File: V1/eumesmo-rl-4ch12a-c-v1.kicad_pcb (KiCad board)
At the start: 2 copper layers, 68 x 67.8 mm, 29 parts, among them J1 250-202, J2 250-204, J3 DB142V-5.08-6P, J4 DB142V-5.08-6P, K1 Songle_SRD_1C, K2 Songle_SRD_1C, K3 Songle_SRD_1C, K4 Songle_SRD_1C

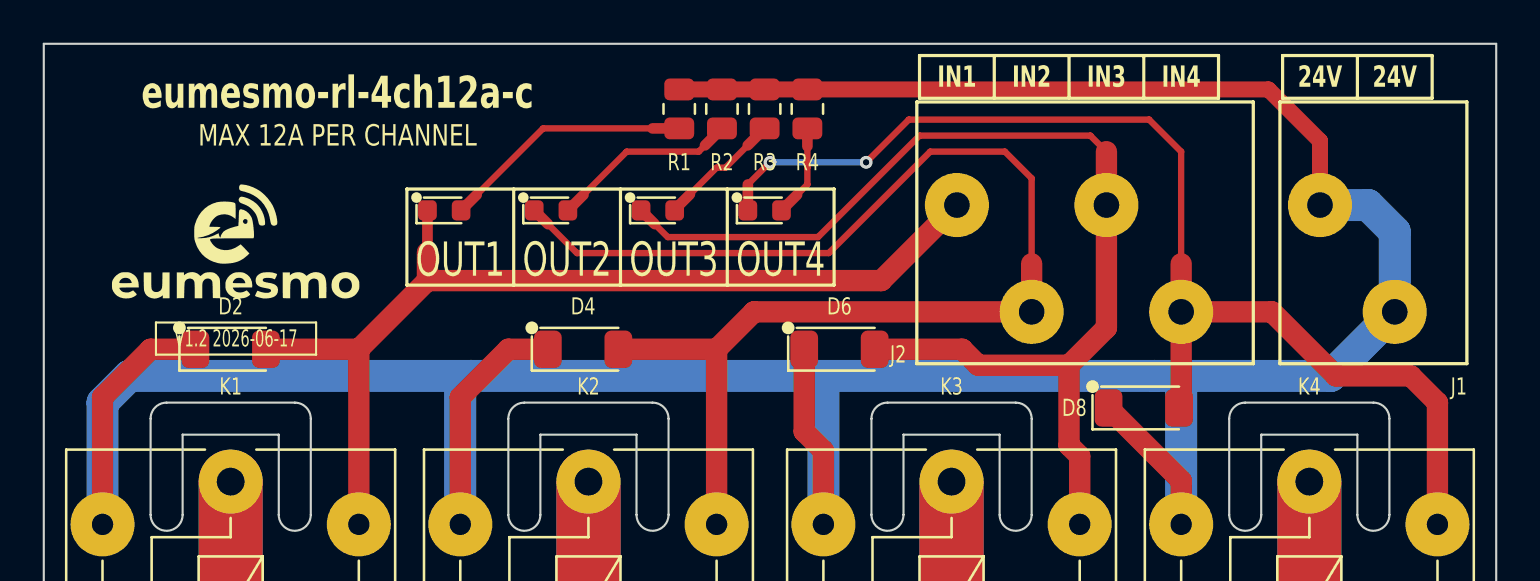
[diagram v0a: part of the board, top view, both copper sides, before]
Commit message: Repo renamed.
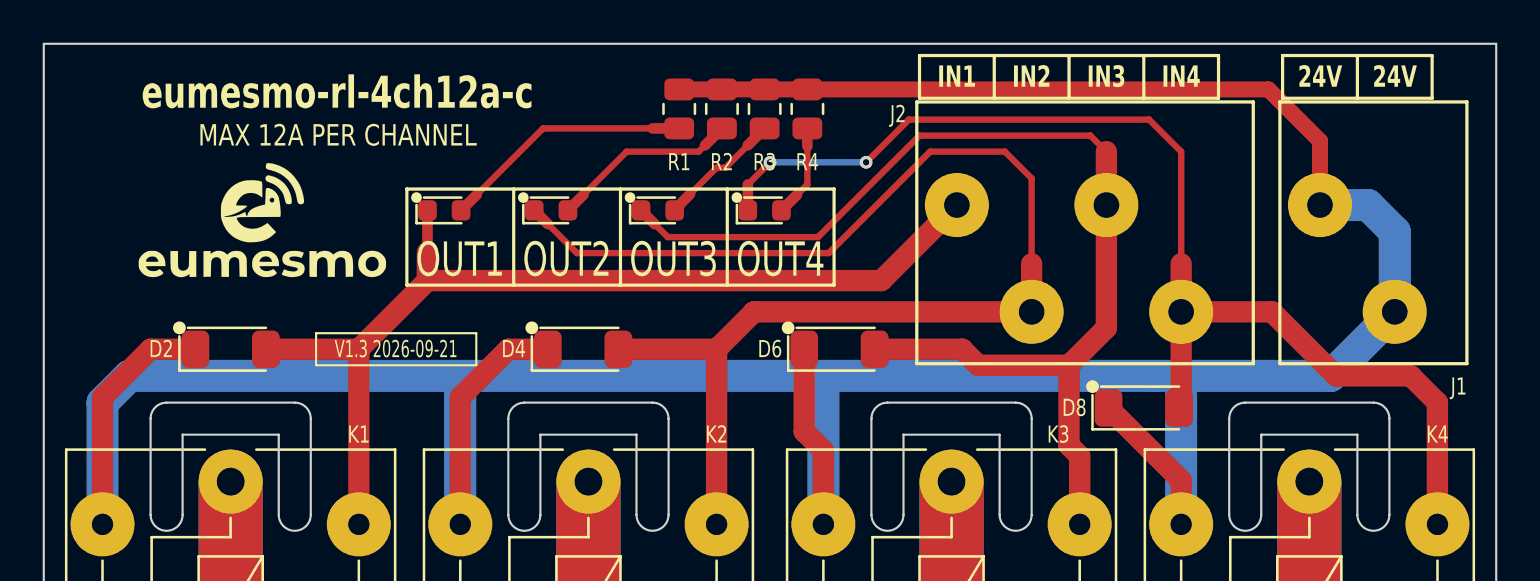
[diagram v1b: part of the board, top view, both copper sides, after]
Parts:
- moved G*** 1.60 mm to (135.2, 70.5)
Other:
- board text added: "V1.3 2026-09-21"
- board text removed: "V1.2 2026-06-17"

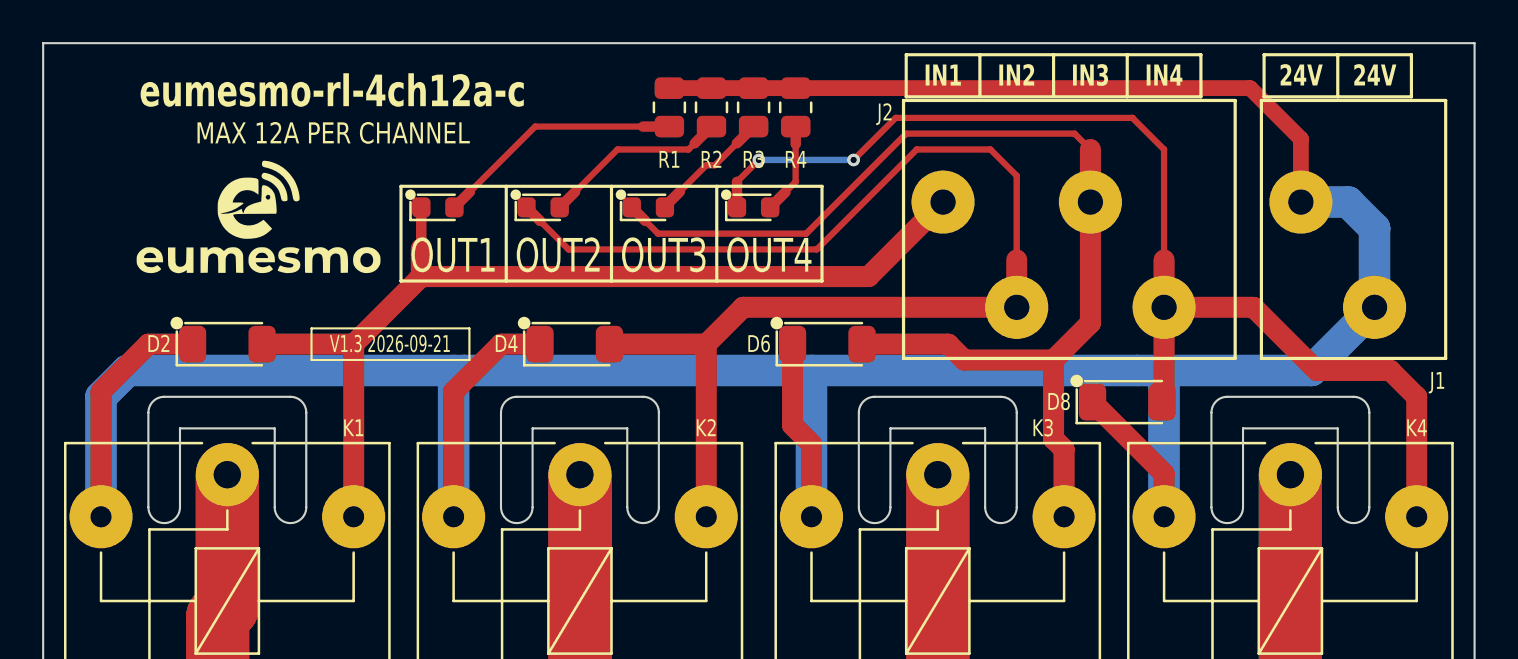
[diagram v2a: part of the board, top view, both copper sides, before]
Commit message: Repositined terminal blocks
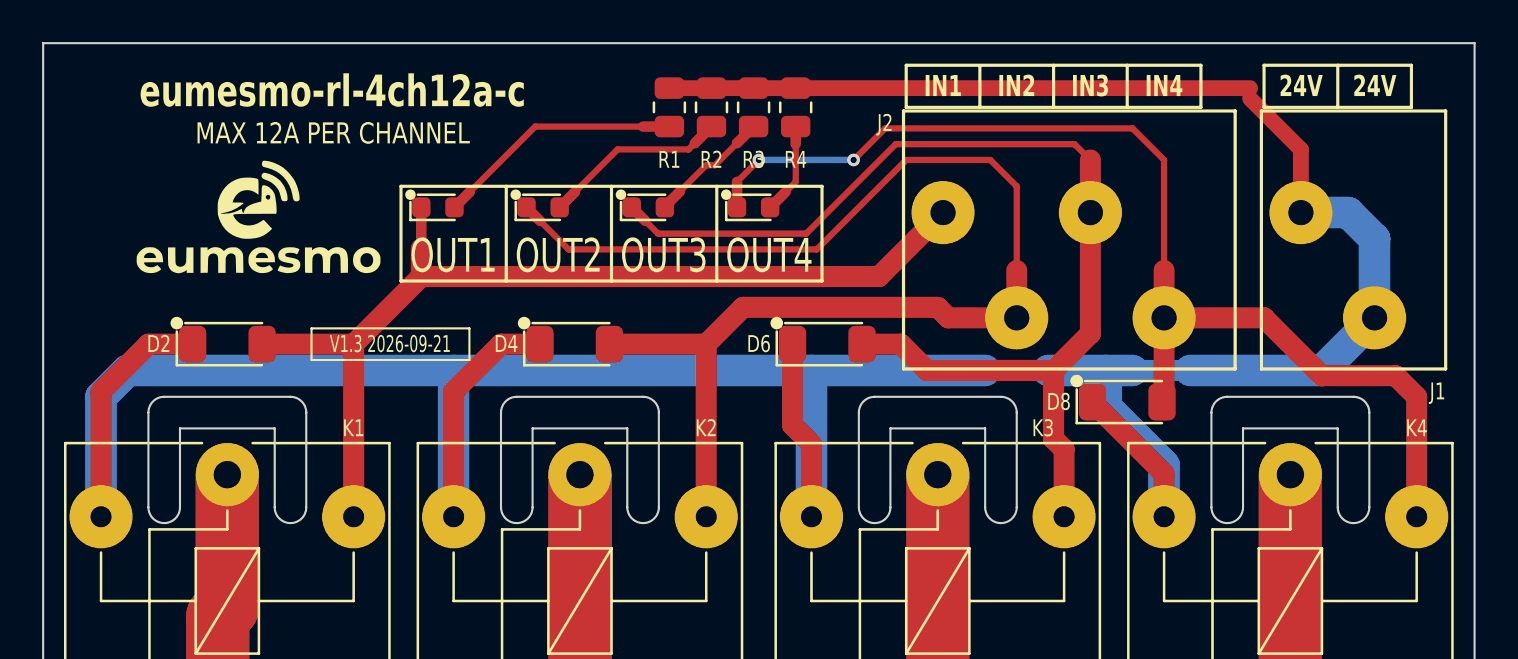
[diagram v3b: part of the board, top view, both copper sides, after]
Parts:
- moved J1 0.50 mm to (186.5, 72.8)
- moved J2 0.50 mm to (173.0, 72.8)
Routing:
- net +24V: track 168.2 -> 169.2 mm

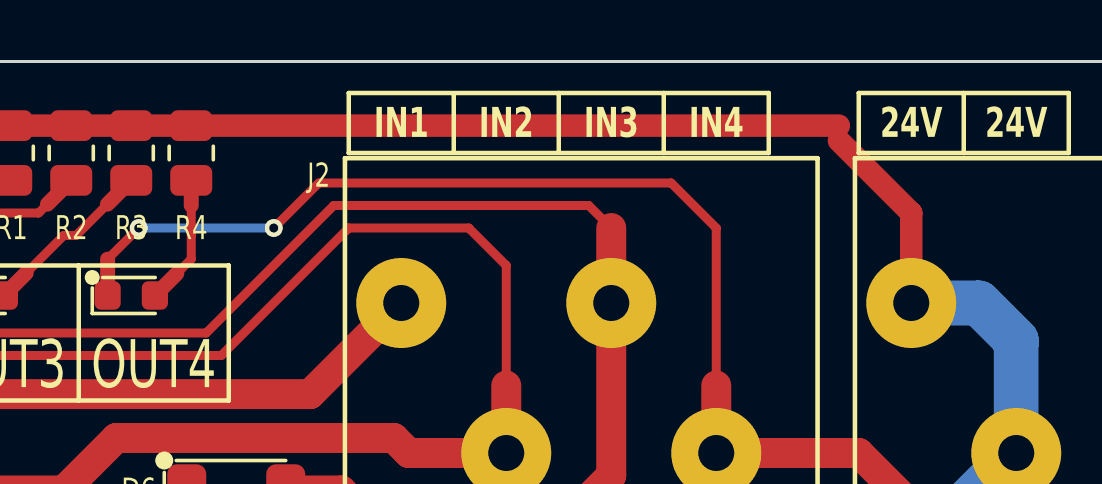
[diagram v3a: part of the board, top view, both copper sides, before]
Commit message: Replaced Wago connectors for other brand, no stock.
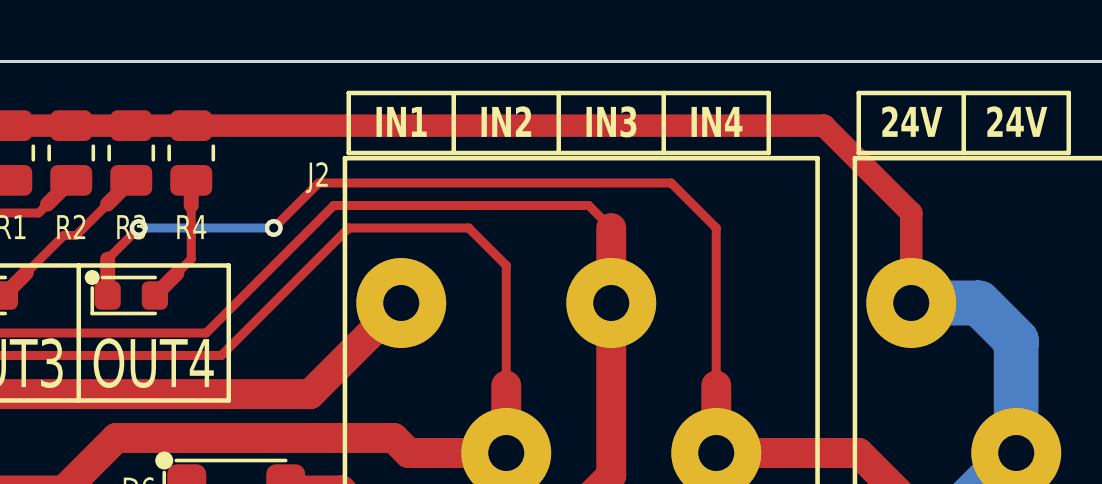
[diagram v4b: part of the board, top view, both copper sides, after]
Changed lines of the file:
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@@
 			)
 		)
-		(property "Mfr" "Wago"
+		(property "Mfr" "Cixi Kefa Elec"
 			(at 0 0 180)
 			(unlocked yes)
@@
 			)
 		)
-		(property "LCSC Part #" "C2765063"
+		(property "LCSC Part #" "C475156"
 			(at 0 0 180)
 			(unlocked yes)
@@
 			)
 		)
-		(property "Mfr PN" "250-204"
+		(property "Mfr PN" "KF250-3.5-4P-1"
 			(at 0 0 180)
 			(unlocked yes)
@@
 			)
 		)
-		(property "Vendor PN" "C2765063"
+		(property "Vendor PN" "C475156"
 			(at 0 0 180)
 			(unlocked yes)
@@
 			)
 		)
-		(property "Mfr" "Wago"
+		(property "Mfr" "Cixi Kefa Elec"
 			(at 0 0 180)
 			(unlocked yes)
@@
 			)
 		)
-		(property "LCSC Part #" "C2765061"
+		(property "LCSC Part #" "C475154"
 			(at 0 0 180)
 			(unlocked yes)
@@
 			)
 		)
-		(property "Mfr PN" "250-202"
+		(property "Mfr PN" "KF250-3.5-2P-1"
 			(at 0 0 180)
 			(unlocked yes)
@@
 			)
 		)
-		(property "Vendor PN" "C2765061"
+		(property "Vendor PN" "C475154"
 			(at 0 0 180)
 			(unlocked yes)
@@
 	)
 	(segment
-		(start 184.75 67.25)
-		(end 184.75 70.25)
-		(width 0.75)
-		(layer "F.Cu")
-		(net "+24V")
-	)
-	(segment
 		(start 160.75 64.3375)
 		(end 158.75 64.3375)
@@
 	)
 	(segment
+		(start 160.75 64.3375)
+		(end 181.8375 64.3375)
+		(width 0.75)
+		(layer "F.Cu")
+		(net "+24V")
+	)
+	(segment
 		(start 178.25 82.65)
 		(end 174.85 79.25)
@@
 	)
 	(segment
-		(start 160.75 64.3375)
-		(end 182.3375 64.3375)
-		(width 0.75)
-		(layer "F.Cu")
-		(net "+24V")
-	)
-	(segment
 		(start 156.75 64.3375)
 		(end 154.75 64.3375)
@@
 	)
 	(segment
-		(start 182.3375 64.8375)
-		(end 184.75 67.25)
+		(start 184.75 67.25)
+		(end 184.75 70.25)
 		(width 0.75)
 		(layer "F.Cu")
@@
 		(layer "F.Cu")
 		(net "+24V")
+	)
+	(segment
+		(start 181.8375 64.3375)
+		(end 184.75 67.25)
+		(width 0.75)
+		(layer "F.Cu")
+		(net "+24V")
